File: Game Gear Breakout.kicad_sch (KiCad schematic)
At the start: 8 parts, among them J1 GG Edge Connector, J2 GG Edge Connector, J3 ROM Chip

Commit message: starting pcb
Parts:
- added D1: +5V, LED_SMD:LED_1206_3216Metric_Pad1.42x1.75mm_HandSolder, symbol Device:LED_Small
- added D2: +34V, LED_SMD:LED_1206_3216Metric_Pad1.42x1.75mm_HandSolder, symbol Device:LED_Small
- added TP1, TP2: TestPoint, TestPoint:TestPoint_Pad_2.0x2.0mm, symbol Connector:TestPoint
- C1, C2: value C_Small -> 1u; footprint (none) -> Capacitor_SMD:C_0805_2012Metric_Pad1.18x1.45mm_HandSolder
- J2: renamed from J1; value GG Edge Connector -> Logic Analyzer
- R1: value R_Small -> 1k; footprint (none) -> Resistor_SMD:R_0805_2012Metric_Pad1.20x1.40mm_HandSolder
- R2: value R_Small -> 10k; footprint (none) -> Resistor_SMD:R_0805_2012Metric_Pad1.20x1.40mm_HandSolder
- renumbered J2 to J1
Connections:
- net +34V: now also R2.1, TP2.1
- net +5V: now also C1.1, C2.1, R1.1, TP1.1
- net A11: now also J3.23 (Pin_23)
- net A8: now also J3.25 (Pin_25)
- net A9: now also J3.24 (Pin_24)
- net GND: now also C1.2, C2.2, D1.1 (K), D2.1 (K); no longer J2.41 (Pin_41)
- net ~{CE}: no longer J3.20 (Pin_20)
- net ~{M0-7}: now also J3.20 (Pin_20)
- net ~{RD}: now also J3.22 (Pin_22)
- net at R2.2: now also D2.2 (A)
- net at R1.2: now also D1.2 (A)
- net GND? renamed Pin 41
- net Pin 41: now also J2.41 (Pin_41)
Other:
- moved on the sheet: C1, C2

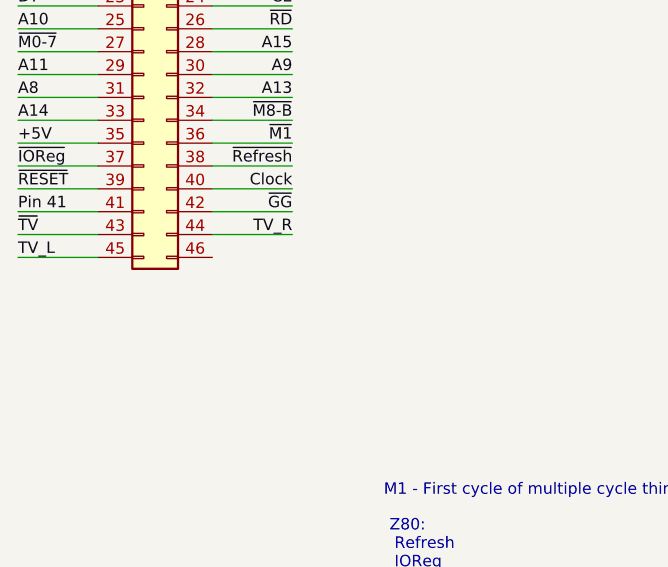
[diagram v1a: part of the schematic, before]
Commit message: added gnd to pin 46 of LA
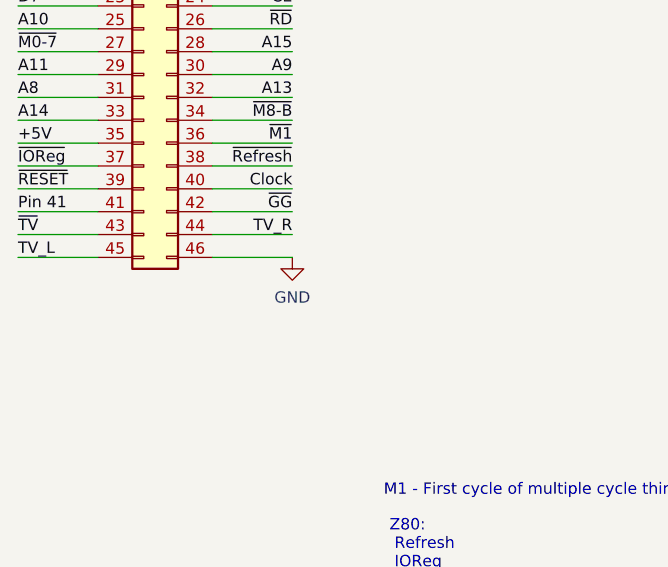
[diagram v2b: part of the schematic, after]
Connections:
- net GND: now also J2.46 (Pin_46)
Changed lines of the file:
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@@
     (stroke (width 0) (type default) (color 0 0 0 0))
   )
+  (wire (pts (xy 41.91 78.105) (xy 50.8 78.105))
+    (stroke (width 0) (type default) (color 0 0 0 0))
+  )
   (wire (pts (xy 41.91 22.225) (xy 50.8 22.225))
     (stroke (width 0) (type default) (color 0 0 0 0))
@@
     (pin "1")
   )
+  (symbol (lib_id "power:GND") (at 50.8 78.105 0) (unit 1)
+    (in_bom yes) (on_board yes) (fields_autoplaced)
+    (property "Reference" "#PWR?" (id 0) (at 50.8 84.455 0)
+      (effects (font (size 1.27 1.27)) hide)
+    )
+    (property "Value" "GND" (id 1) (at 50.8 82.55 0))
+    (property "Footprint" "" (id 2) (at 50.8 78.105 0)
+      (effects (font (size 1.27 1.27)) hide)
+    )
+    (property "Datasheet" "" (id 3) (at 50.8 78.105 0)
+      (effects (font (size 1.27 1.27)) hide)
+    )
+    (pin "1")
+  )
   (symbol (lib_id "Device:R_Small") (at 193.04 25.4 0) (unit 1)
     (in_bom yes) (on_board yes) (fields_autoplaced)
@@
       (reference "#PWR08") (unit 1) (value "GND") (footprint "")
     )
+    (path "/d5bb216b-8b9e-4512-88d2-27c7f0d7eba6"
+      (reference "#PWR?") (unit 1) (value "GND") (footprint "")
+    )
     (path "/af780954-8141-44ad-8d3a-ddf814b81c6f"

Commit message: bottom routed (try #1)
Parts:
- removed C2: 1u, Capacitor_SMD:C_0805_2012Metric_Pad1.18x1.45mm_HandSolder, symbol Device:C_Small
- removed TP1, TP2: TestPoint, TestPoint:TestPoint_Pad_2.0x2.0mm, symbol Connector:TestPoint
- added PEG1, PEG2: MountingHole, MountingHole:MountingHole_2.7mm_M2.5, symbol Mechanical:MountingHole
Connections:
- net GND: no longer J1.41 (Pin_41)
- net Pin 41: now also J1.41 (Pin_41)

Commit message: rev1 layout done?
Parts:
- added TP1, TP2, TP3, TP?: TestPoint, My Libraries:Harwin-S1751-46-Test-Point, symbol Connector:TestPoint
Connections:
- net +5V: now also TP?.1
- net GND: now also TP1.1, TP2.1, TP3.1
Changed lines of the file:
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@@
 (kicad_sch (version 20211123) (generator eeschema)
   (paper "A4")
+  (junction (at 31.115 98.425) (diameter 0) (color 0 0 0 0)
+  )
   (wire (pts (xy 116.205 36.83) (xy 125.095 36.83))
     (stroke (width 0) (type default) (color 0 0 0 0))
@@
     (stroke (width 0) (type default) (color 0 0 0 0))
   )
+  (wire (pts (xy 18.415 98.425) (xy 31.115 98.425))
+    (stroke (width 0) (type default) (color 0 0 0 0))
+  )
+  (wire (pts (xy 31.115 98.425) (xy 31.115 101.6))
+    (stroke (width 0) (type default) (color 0 0 0 0))
+  )
   (wire (pts (xy 116.205 52.07) (xy 125.095 52.07))
     (stroke (width 0) (type default) (color 0 0 0 0))
@@
     (stroke (width 0) (type default) (color 0 0 0 0))
   )
+  (wire (pts (xy 31.115 98.425) (xy 43.18 98.425))
+    (stroke (width 0) (type default) (color 0 0 0 0))
+  )
   (wire (pts (xy 116.205 82.55) (xy 125.095 82.55))
     (stroke (width 0) (type default) (color 0 0 0 0))
@@
     (effects (font (size 1.27 1.27)) (justify left bottom))
   )
+  (symbol (lib_id "Connector:TestPoint") (at 43.18 98.425 0) (unit 1)
+    (in_bom yes) (on_board yes) (fields_autoplaced)
+    (property "Reference" "TP3" (id 0) (at 45.72 93.8529 0)
+      (effects (font (size 1.27 1.27)) (justify left))
+    )
+    (property "Value" "TestPoint" (id 1) (at 45.72 96.3929 0)
+      (effects (font (size 1.27 1.27)) (justify left))
+    )
+    (property "Footprint" "My Libraries:Harwin-S1751-46-Test-Point" (id 2) (at 48.26 98.425 0)
+      (effects (font (size 1.27 1.27)) hide)
+    )
+    (property "Datasheet" "~" (id 3) (at 48.26 98.425 0)
+      (effects (font (size 1.27 1.27)) hide)
+    )
+    (pin "1")
+  )
   (symbol (lib_id "Mechanical:MountingHole") (at 45.72 172.72 0) (unit 1)
     (in_bom yes) (on_board yes) (fields_autoplaced)
@@
     (pin "9")
   )
+  (symbol (lib_id "Connector:TestPoint") (at 172.72 24.765 270) (unit 1)
+    (in_bom yes) (on_board yes) (fields_autoplaced)
+    (property "Reference" "TP?" (id 0) (at 177.2921 27.305 0)
+      (effects (font (size 1.27 1.27)) (justify left))
+    )
+    (property "Value" "TestPoint" (id 1) (at 174.7521 27.305 0)
+      (effects (font (size 1.27 1.27)) (justify left))
+    )
+    (property "Footprint" "My Libraries:Harwin-S1751-46-Test-Point" (id 2) (at 172.72 29.845 0)
+      (effects (font (size 1.27 1.27)) hide)
+    )
+    (property "Datasheet" "~" (id 3) (at 172.72 29.845 0)
+      (effects (font (size 1.27 1.27)) hide)
+    )
+    (pin "1")
+  )
+  (symbol (lib_id "Connector:TestPoint") (at 18.415 98.425 0) (unit 1)
+    (in_bom yes) (on_board yes) (fields_autoplaced)
+    (property "Reference" "TP1" (id 0) (at 20.955 93.8529 0)
+      (effects (font (size 1.27 1.27)) (justify left))
+    )
+    (property "Value" "TestPoint" (id 1) (at 20.955 96.3929 0)
+      (effects (font (size 1.27 1.27)) (justify left))
+    )
+    (property "Footprint" "My Libraries:Harwin-S1751-46-Test-Point" (id 2) (at 23.495 98.425 0)
+      (effects (font (size 1.27 1.27)) hide)
+    )
+    (property "Datasheet" "~" (id 3) (at 23.495 98.425 0)
+      (effects (font (size 1.27 1.27)) hide)
+    )
+    (pin "1")
+  )
   (symbol (lib_id "power:+5V") (at 232.41 29.21 0) (unit 1)
     (in_bom yes) (on_board yes) (fields_autoplaced)
@@
     (pin "2")
   )
+  (symbol (lib_id "power:+5V") (at 172.72 24.765 0) (unit 1)
+    (in_bom yes) (on_board yes) (fields_autoplaced)
+    (property "Reference" "#PWR?" (id 0) (at 172.72 28.575 0)
+      (effects (font (size 1.27 1.27)) hide)
+    )
+    (property "Value" "+5V" (id 1) (at 172.7201 26.035 90)
+      (effects (font (size 1.27 1.27)) (justify right))
+    )
+    (property "Footprint" "" (id 2) (at 172.72 24.765 0)
+      (effects (font (size 1.27 1.27)) hide)
+    )
+    (property "Datasheet" "" (id 3) (at 172.72 24.765 0)
+      (effects (font (size 1.27 1.27)) hide)
+    )
+    (pin "1")
+  )
+  (symbol (lib_id "Connector:TestPoint") (at 31.115 98.425 0) (unit 1)
+    (in_bom yes) (on_board yes) (fields_autoplaced)
+    (property "Reference" "TP2" (id 0) (at 33.655 93.8529 0)
+      (effects (font (size 1.27 1.27)) (justify left))
+    )
+    (property "Value" "TestPoint" (id 1) (at 33.655 96.3929 0)
+      (effects (font (size 1.27 1.27)) (justify left))
+    )
+    (property "Footprint" "My Libraries:Harwin-S1751-46-Test-Point" (id 2) (at 36.195 98.425 0)
+      (effects (font (size 1.27 1.27)) hide)
+    )
+    (property "Datasheet" "~" (id 3) (at 36.195 98.425 0)
+      (effects (font (size 1.27 1.27)) hide)
+    )
+    (pin "1")
+  )
   (symbol (lib_id "Device:C_Small") (at 232.41 33.02 0) (unit 1)
     (in_bom yes) (on_board yes) (fields_autoplaced)
@@
     (pin "1")
   )
+  (symbol (lib_id "power:GND") (at 31.115 101.6 0) (unit 1)
+    (in_bom yes) (on_board yes) (fields_autoplaced)
+    (property "Reference" "#PWR0102" (id 0) (at 31.115 107.95 0)
+      (effects (font (size 1.27 1.27)) hide)
+    )
+    (property "Value" "GND" (id 1) (at 31.115 106.68 0))
+    (property "Footprint" "" (id 2) (at 31.115 101.6 0)
+      (effects (font (size 1.27 1.27)) hide)
+    )
+    (property "Datasheet" "" (id 3) (at 31.115 101.6 0)
+      (effects (font (size 1.27 1.27)) hide)
+    )
+    (pin "1")
+  )
   (sheet_instances
     (path "/" (page "1"))
@@
       (reference "#PWR0101") (unit 1) (value "GND") (footprint "")
     )
+    (path "/ffe96cdd-5fcd-4b87-9e02-a6841a576238"
+      (reference "#PWR0102") (unit 1) (value "GND") (footprint "")
+    )
+    (path "/96a90aff-c65c-4fd2-a19a-78d6d574a31a"
+      (reference "#PWR?") (unit 1) (value "+5V") (footprint "")
+    )
     (path "/af780954-8141-44ad-8d3a-ddf814b81c6f"
       (reference "C1") (unit 1) (value "1u") (footprint "Capacitor_SMD:C_0805_2012Metric_Pad1.18x1.45mm_HandSolder")
@@
       (reference "R2") (unit 1) (value "10k") (footprint "Resistor_SMD:R_0805_2012Metric_Pad1.20x1.40mm_HandSolder")
     )
+    (path "/5490f0fc-65f6-4ce3-a62f-1158b9a106ce"
+      (reference "TP1") (unit 1) (value "TestPoint") (footprint "My Libraries:Harwin-S1751-46-Test-Point")
+    )
+    (path "/98de8721-4fc4-44fe-a3dc-373ddfa1a2f1"
+      (reference "TP2") (unit 1) (value "TestPoint") (footprint "My Libraries:Harwin-S1751-46-Test-Point")
+    )
+    (path "/05437a29-bc48-492a-a750-d3b834665ac5"
+      (reference "TP3") (unit 1) (value "TestPoint") (footprint "My Libraries:Harwin-S1751-46-Test-Point")
+    )
+    (path "/31aebd13-dcb6-46b9-ab66-dfafd589c281"
+      (reference "TP?") (unit 1) (value "TestPoint") (footprint "My Libraries:Harwin-S1751-46-Test-Point")
+    )
   )

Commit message: v1 submitting to fab
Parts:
- gave numbers to parts that had none: 1
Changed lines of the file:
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@@
   (symbol (lib_id "Connector:TestPoint") (at 172.72 24.765 270) (unit 1)
     (in_bom yes) (on_board yes) (fields_autoplaced)
-    (property "Reference" "TP?" (id 0) (at 177.2921 27.305 0)
+    (property "Reference" "TP4" (id 0) (at 177.2921 27.305 0)
       (effects (font (size 1.27 1.27)) (justify left))
     )
@@
   (symbol (lib_id "power:+5V") (at 172.72 24.765 0) (unit 1)
     (in_bom yes) (on_board yes) (fields_autoplaced)
-    (property "Reference" "#PWR?" (id 0) (at 172.72 28.575 0)
+    (property "Reference" "#PWR0103" (id 0) (at 172.72 28.575 0)
       (effects (font (size 1.27 1.27)) hide)
     )
@@
     )
     (path "/96a90aff-c65c-4fd2-a19a-78d6d574a31a"
-      (reference "#PWR?") (unit 1) (value "+5V") (footprint "")
+      (reference "#PWR0103") (unit 1) (value "+5V") (footprint "")
     )
     (path "/af780954-8141-44ad-8d3a-ddf814b81c6f"
@@
     )
     (path "/31aebd13-dcb6-46b9-ab66-dfafd589c281"
-      (reference "TP?") (unit 1) (value "TestPoint") (footprint "My Libraries:Harwin-S1751-46-Test-Point")
-    )
-  )
+      (reference "TP4") (unit 1) (value "TestPoint") (footprint "My Libraries:Harwin-S1751-46-Test-Point")
+    )
+  )

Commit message: gerbs and pdf of schematic (v1)
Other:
- company: (none) -> twitch.tv/baldengineer
- title: (none) -> Game Gear Cart Breakout
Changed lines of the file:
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@@
 (kicad_sch (version 20211123) (generator eeschema)
   (paper "A4")
+  (title_block
+    (title "Game Gear Cart Breakout")
+    (date "2022-12-02")
+    (rev "1")
+    (company "twitch.tv/baldengineer")
+  )
   (junction (at 31.115 98.425) (diameter 0) (color 0 0 0 0)
   )
